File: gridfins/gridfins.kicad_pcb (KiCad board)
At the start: 4 copper layers, 195 parts, among them IC1 2536030320001, J1 RBUS, J2 USB_C_Receptacle_USB2.0, J3 ServoCH0, J4 ServoCH1, J5 ServoCH2, J6 ST1W008S4TR2000, J8 1053131104, Q1 SSM3K15AMFV,L3F, Q3 DMP3099, Q4 SSM3K15AMFV,L3F, Q5 BSZ025N04LS, Q6 BSZ025N04LS, U1 ESP32-S3, U10 LM74810, U12 SiC437AED-T1, U2 SN65HVD230, U3 LM66200DRLR, U4 MAX77827AEFD+T, U5 SC4215ASTRT, U6 SiC437AED-T1, U7 DRV8834PWP, U8 MMC5983MA, U9 H3LIS331DLTR, Y1 R940000171

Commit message: feat: Massive changes, board almost ready for review
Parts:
- removed C18: 10uF, Capacitor_SMD:C_0402_1005Metric
- removed D6, D7: ~, Package_TO_SOT_SMD:SOT-353_SC-70-5
- removed JP2, JP3: Conn_01x02_Male, Connector_PinHeader_2.54mm:PinHeader_1x02_P2.54mm_Vertical
- removed TP3: TestPoint, TestPoint:TestPoint_Pad_D1.0mm
- added C30: 10uF, Capacitor_SMD:C_0805_2012Metric, F.Cu at (225.7, 102.0)
- added D3: CPDF3V3UP-HF, iclr:CPD, B.Cu at (249.6, 67.0)
- added G**: orientation_marker, iclr-hw:orientation_marker, F.Cu at (258.4, 46.8)
- added J10: Limit switch 2, Connector_PinHeader_2.54mm:PinHeader_1x02_P2.54mm_Vertical, F.Cu at (230.3, 90.9)
- added J11: Conn_01x03_Pin, Connector_PinHeader_1.00mm:PinHeader_1x03_P1.00mm_Vertical, F.Cu at (242.7, 52.7)
- added J7: Encoder breakout, Connector_PinHeader_2.54mm:PinHeader_2x03_P2.54mm_Vertical, F.Cu at (243.8, 62.2)
- added J9: Limit switch 1, Connector_PinHeader_2.54mm:PinHeader_1x02_P2.54mm_Vertical, F.Cu at (230.3, 81.7)
- added R46: 10k, Resistor_SMD:R_0402_1005Metric, F.Cu at (238.0, 108.9)
- added R47: 10k, Resistor_SMD:R_0402_1005Metric, F.Cu at (230.3, 99.5)
- added R48: 10k, Resistor_SMD:R_0402_1005Metric, F.Cu at (230.7, 79.3)
- added R49: 10k, Resistor_SMD:R_0402_1005Metric, F.Cu at (230.7, 93.3)
- added TP11: TestPoint, TestPoint:TestPoint_Pad_D1.0mm, F.Cu at (228.2, 67.6)
- added TP12: TestPoint, TestPoint:TestPoint_Pad_D1.0mm, F.Cu at (231.7, 98.2)
- added TP13: TestPoint, TestPoint:TestPoint_Pad_D1.0mm, F.Cu at (246.3, 78.9)
- added TP14: TestPoint, TestPoint:TestPoint_Pad_D1.0mm, F.Cu at (245.5, 83.7)
- D4, D5: value ~ -> CPDF3V3UP-HF; footprint Package_TO_SOT_SMD:SOT-353_SC-70-5 -> iclr:CPD; moved to B.Cu
- J1: footprint iclr:Molex_Mini-Fit_Jr_5569-06A2_2x03_P4.20mm_Horizontal -> iclr:Molex_Mini-Fit_Jr_5569-08A2_2x04_P4.20mm_Horizontal
- J6, R25, R26, R27, R30, R56, TP1, TP2, TP25, TP26, TP27, TP4, TP5, TP6, TP7, TP8: moved to B.Cu
- JP1: footprint iclr:SmallerSolderJP -> Capacitor_SMD:C_0603_1608Metric_Pad1.08x0.95mm_HandSolder
- R43, R44: value 0.32 -> 0.5; footprint Resistor_SMD:R_0402_1005Metric -> Resistor_SMD:R_2512_6332Metric
- moved H3 171.8 mm to (254.8, 112.5)
- moved H2 167.6 mm to (254.8, 33.5)
- moved J3 165.7 mm to (252.0, 65.4)
- moved J4 165.7 mm to (252.0, 75.9)
- moved J5 165.7 mm to (252.0, 86.4)
- moved C10 157.9 mm to (251.6, 48.4), turned to 45 degrees
- moved C13 153.0 mm to (250.2, 45.8), turned to -90 degrees
- moved R25 152.1 mm to (249.5, 70.2), turned to -90 degrees
- moved C5 151.8 mm to (243.1, 50.9), turned to -90 degrees
- moved C9 151.2 mm to (245.1, 47.9), turned to 90 degrees
- moved C1 151.2 mm to (243.6, 49.5)
- moved C4 150.8 mm to (242.1, 49.4), turned to -90 degrees
- moved R26 150.7 mm to (249.5, 80.0), turned to -90 degrees
- moved R27 149.8 mm to (249.4, 88.2), turned to -90 degrees
- moved C6 149.6 mm to (245.1, 51.0), turned to 90 degrees
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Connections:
- C3 pad 1: /CHIP_PU -> GND
- C3 pad 2: GND -> /CHIP_PU
- C40 pad 1: +16.8V -> /DeployV
- C48 pad 1: +16.8V -> /DeployV
- C75 pad 1: +16.8V -> /DeployV
- C82 pad 1: +16.8V -> /DeployV
- C85 pad 1: +16.8V -> /DeployV
- C92 pad 1: +16.8V -> /DeployV
- D4 pad 1: /SERVOPWM0 -> GND
- D4 pad 2: Net-(D4-Pad2) -> /SERVOPWM1
- D5 pad 2: Net-(D4-Pad2) -> /SERVOPWM2
- J1 pad 3: RBUS_uC_V -> GND
- J1 pad 4: +16.8V -> RBUS_uC_V
- J1 pad 5: /CAN+ -> /DeployV
- J1 pad 6: /CAN- -> /DeployV
- J8 pad 1: Net-(U7-AOUT1) -> /Linear Actuator/BOUT1
- J8 pad 2: Net-(U7-AOUT2) -> /Linear Actuator/BOUT2
- J8 pad 3: Net-(U7-BOUT2) -> /Linear Actuator/AOUT2
- J8 pad 4: Net-(U7-BOUT1) -> /Linear Actuator/AOUT1
- Q1 pad 1: /BUCK_EN -> /BUCK_EN_H
- Q4 pad 1: /BUCK_EN -> /BUCK_EN_S
- R20 pad 2: /BuckPGOOD -> /BuckPGOOD_H
- R24 pad 2: /BUCK_EN -> /BUCK_EN_H
- R34 pad 2: /BuckPGOOD -> /BuckPGOOD_H
- R45 pad 2: /BuckPGOOD -> /BuckPGOOD_S
- R56 pad 2: +16.8V -> /DeployV
- R58 pad 2: /BuckPGOOD -> /BuckPGOOD_S
- R62 pad 2: /BUCK_EN -> /BUCK_EN_S
- R66 pad 2: +16.8V -> /DeployV
- R7 pad 1: +12V -> +10V
- U1 pad 10: /SD1_CS -> /VSPI_MISO
- U1 pad 13: /VSPI_MISO -> /SD1_CS
- U1 pad 14: /HSPI_MISO -> /ENCODER_CS
- U1 pad 15: /HSPI_MOSI -> /CAN_RX
- U1 pad 16: /HSPI_SCLK -> /CAN_TX
- U1 pad 17: /IMU1_CS -> /HSIDE_EN
- U1 pad 18: /IMU2_CS -> /BUCK_EN_H
- U1 pad 19: /MAG_CS -> /BUCK_EN_S
- U1 pad 21: /STEP/BENBL -> /SERVOPWM2
- U1 pad 22: /NSLEEP -> /SERVOPWM1
- U1 pad 23: /M0/APHASE -> /SERVOPWM0
- U1 pad 24: /DIR/BPHASE -> /BUS_VMON
- U1 pad 27: /NENBL/AENBL -> /M0/APHASE
- U1 pad 36: unconnected-(U1-SPICLK_N/GPIO48-Pad36) -> /M1
- U1 pad 37: unconnected-(U1-SPICLK_P/GPIO47-Pad37) -> /Fault
- U1 pad 38: unconnected-(U1-GPIO33-Pad38) -> /NSLEEP
- U1 pad 39: /SERVOPWM0 -> /DIR/BPHASE
- U1 pad 40: /SERVOPWM1 -> /STEP/BENBL
- U1 pad 41: /SERVOPWM2 -> /NENBL/AENBL
- U1 pad 42: /HSIDE_EN -> /HSPI_MOSI
- U1 pad 43: /ENCODER_CS -> /HSPI_SCLK
- U1 pad 44: unconnected-(U1-MTCK/JTAG/GPIO39-Pad44) -> /HSPI_MISO
- U1 pad 45: unconnected-(U1-MTDO/JTAG/GPIO40-Pad45) -> /Switch_1
- U1 pad 47: unconnected-(U1-MTDI/JTAG/GPIO41-Pad47) -> /IMU1_CS
- U1 pad 48: unconnected-(U1-MTMS/JTAG/GPIO42-Pad48) -> /IMU2_CS
- U1 pad 51: /BUCK_EN -> /MAG_CS
- U1 pad 6: /BUS_VMON -> /Switch_2
- U12 pad 1: +16.8V -> /DeployV
- U12 pad 14: /BuckPGOOD -> /BuckPGOOD_S
- U12 pad 2: +16.8V -> /DeployV
- U12 pad 22: +16.8V -> /DeployV
- U12 pad 26: +16.8V -> /DeployV
- U6 pad 1: +16.8V -> /DeployV
- U6 pad 14: /BuckPGOOD -> /BuckPGOOD_H
- U6 pad 2: +16.8V -> /DeployV
- U6 pad 22: +16.8V -> /DeployV
- U6 pad 26: +16.8V -> /DeployV
- U7 pad 14: /Linear Actuator/VINT -> /M1
- U7 pad 15: GND -> Net-(U7-CONFIG)
- U7 pad 16: unconnected-(U7-NFAULT-Pad16) -> /Fault
- U7 pad 4: Net-(U7-AOUT1) -> /Linear Actuator/AOUT1
- U7 pad 6: Net-(U7-AOUT2) -> /Linear Actuator/AOUT2
- U7 pad 7: Net-(U7-BOUT2) -> /Linear Actuator/BOUT2
- U7 pad 9: Net-(U7-BOUT1) -> /Linear Actuator/BOUT1
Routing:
- net /BUS_VMON: track 0.00 -> 87.1 mm, vias 0 -> 2
- net /HSIDE_EN: track 0.00 -> 77.9 mm, vias 0 -> 2
- net /Switch_1: track 0.00 -> 77.2 mm, vias 0 -> 2
- net /NSLEEP: track 0.00 -> 76.6 mm
- net /Fault: track 0.00 -> 69.3 mm
- net /NENBL/AENBL: track 0.00 -> 69.3 mm, vias 0 -> 2
- net /STEP/BENBL: track 0.00 -> 67.9 mm, vias 0 -> 2
- net /M1: track 0.00 -> 67.7 mm
- net /DIR/BPHASE: track 0.00 -> 64.3 mm, vias 0 -> 2
- net /M0/APHASE: track 0.00 -> 63.9 mm
- net /Switch_2: track 0.00 -> 58.4 mm, vias 0 -> 1
- net +3V3: track 0.00 -> 51.3 mm, vias 1 -> 23
- net /HSPI_MISO: track 0.00 -> 33.2 mm, vias 0 -> 5
- net /Data+: track 0.00 -> 33.1 mm, vias 0 -> 2
- net /SERVOPWM2: track 0.00 -> 32.3 mm, vias 0 -> 1
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- added copper zone on B.Cu, net +10V
- added copper zone on F.Cu, net +10V
- added copper zone on In2.Cu, net +3V3
- added copper zone on F.Cu, net +7.4V
- added copper zone on F.Cu, net /Buck_SERVO/SW
- added copper zone on B.Cu, net /DeployV
- added copper zone on F.Cu, net /DeployV
- added copper zone on In2.Cu, net /DeployV
- added copper zone on B.Cu, net /Linear Actuator/AOUT1
- added copper zone on F.Cu, net /Linear Actuator/AOUT1
- added copper zone on B.Cu, net /Linear Actuator/AOUT2
- added copper zone on F.Cu, net /Linear Actuator/AOUT2
- added copper zone on B.Cu, net /Linear Actuator/BOUT1
- added copper zone on F.Cu, net /Linear Actuator/BOUT1
- added copper zone on B.Cu, net /Linear Actuator/BOUT2
- added copper zone on F.Cu, net /Linear Actuator/BOUT2
- added copper zone on F.Cu, net /Linear Actuator/VREFO
- added copper zone on B.Cu, net /VOUTSwitch
- added copper zone on F.Cu, net /VOUTSwitch
- added copper zone on B.Cu, net /master high side switch/C
- added copper zone on F.Cu, net /master high side switch/C
- added copper zone on B.Cu, net GND
- added copper zone on In1.Cu, net GND
- added copper zone on F.Cu, net Net-(C6-Pad1)
- added copper zone on B.Cu, net Net-(C65-Pad2)
- added copper zone on B.Cu, net Net-(C90-Pad2)
- added copper zone on F.Cu, net Net-(JP1-B)
- added copper zone on F.Cu, net Net-(U7-AISEN)
- added copper zone on F.Cu, net Net-(U7-BISEN)
- removed copper zone on F.Cu, net +16.8V
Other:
- board outline added: 47.1 x 85.5 mm
- board text added: "LEDs"
- board text added: "connect to Voutswitch via"

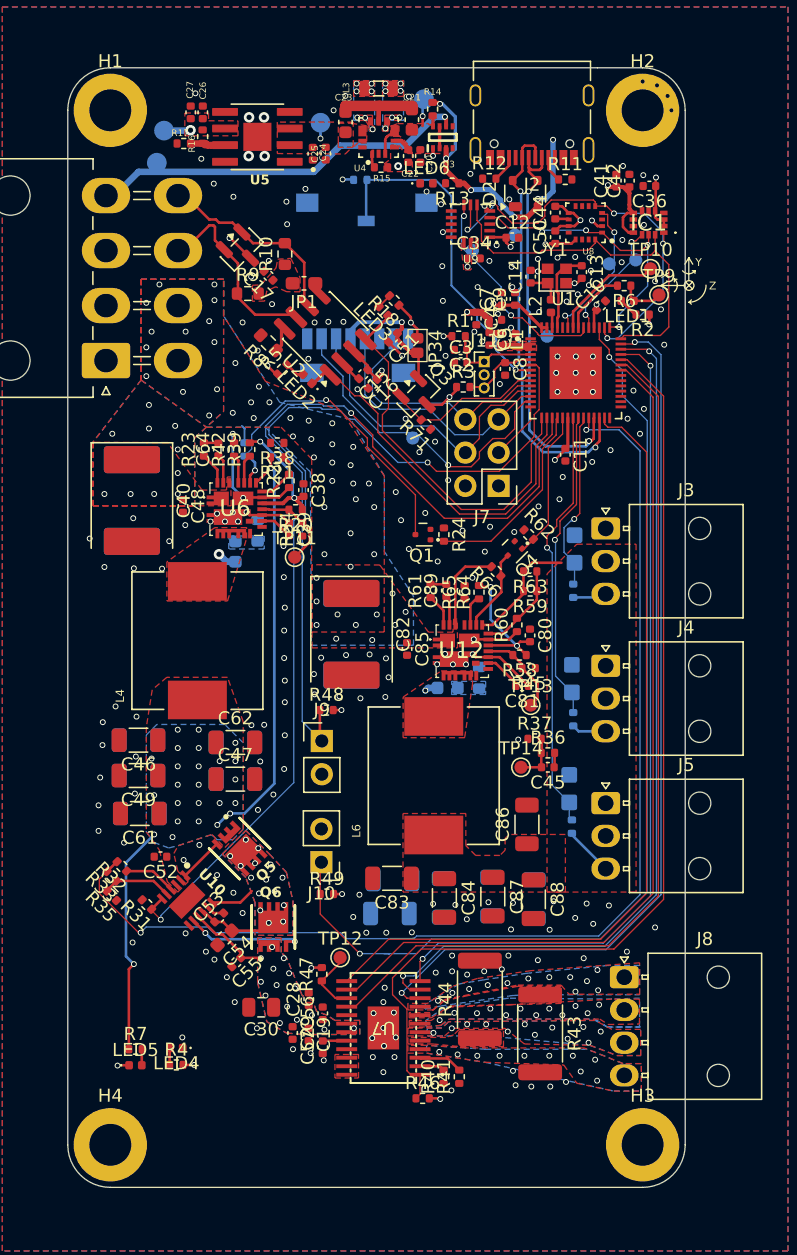
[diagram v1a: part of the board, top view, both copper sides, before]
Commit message: feat: A few more changes, mainly fixing copper pours and DRC erros. Still need to change buck inductors to wuerth ones + route end stop switch traces better.
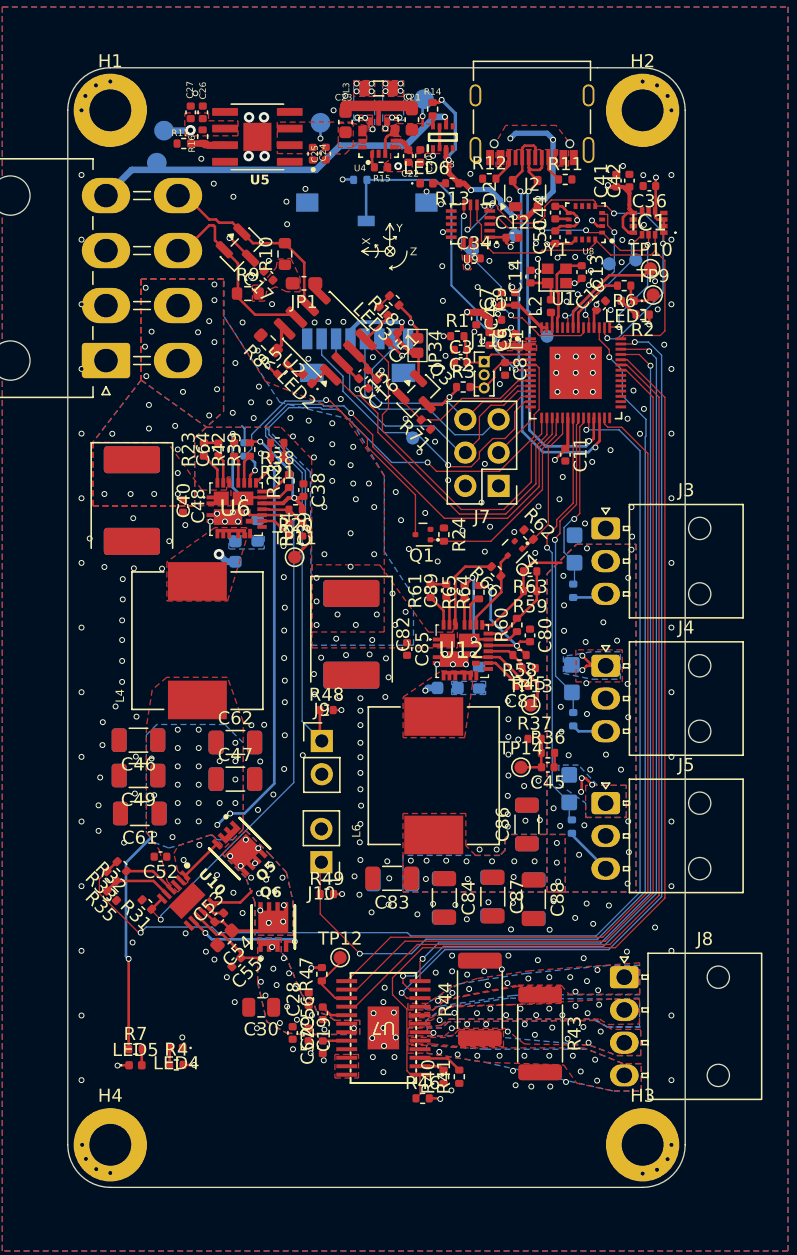
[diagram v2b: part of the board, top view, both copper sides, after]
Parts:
- moved G** 23.0 mm to (235.5, 44.2)
- moved C94 12.5 mm to (246.0, 88.0), turned to 90 degrees
- moved TP9 0.45 mm to (255.6, 47.6)
- moved R1 0.10 mm to (240.7, 50.7)
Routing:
- net GND: track 45.0 -> 214.7 mm, vias 223 -> 314
- net VBUS: track 22.3 -> 26.3 mm, vias 6 -> 7
- net Net-(U7-VCP): track 0.00 -> 2.09 mm
- net Net-(U12-_MODE_1): track 0.00 -> 1.99 mm
- net /Buck_H_bridge/FB: track 4.06 -> 5.16 mm
- net /BUCK_EN_H: track 15.1 -> 16.2 mm
- net Net-(LED6-A): track 0.00 -> 0.97 mm
- net +10V: track 50.0 -> 50.8 mm
- net /Switch_1: track 77.2 -> 76.6 mm
- net /DeployV: vias 60 -> 59
- net +7.4V: vias 0 -> 39
- added copper zone on B.Cu, net +7.4V
- added copper zone on F.Cu, net VBUS
- removed copper zone on In2.Cu, net /DeployV

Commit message: feat: Ready for first review, made a mockup name etc
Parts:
- added G***: LOGO, LOGO, F.Cu at (218.3, 103.6)
- added G***: LOGO, LOGO, B.Cu at (234.7, 85.3)
- added LOGO1: ICLR LOGO, iclr:iclr_logo_estd2018_10mm, B.Cu at (245.8, 36.3)
- moved R4 8.49 mm to (214.7, 99.2), turned to 90 degrees
- moved R7 6.51 mm to (213.5, 99.2), turned to -90 degrees
- moved LED5 2.29 mm to (216.0, 104.1)
- moved TP8 1.65 mm to (228.7, 34.9)
- moved LED4 1.54 mm to (217.9, 104.3)
- moved R40 1.23 mm to (239.6, 108.5)
- moved R41 1.15 mm to (240.8, 108.4)
- moved TP1 0.95 mm to (246.6, 50.7)
- moved R46 0.93 mm to (237.1, 108.9), turned to 180 degrees
- moved G** 0.85 mm to (235.1, 43.5), turned to 180 degrees
- moved U3 0.69 mm to (239.4, 36.2)
- moved C22 0.69 mm to (236.8, 37.6)
- moved U4 0.69 mm to (234.5, 36.2)
- moved C20 0.69 mm to (237.7, 37.6)
- moved C21 0.69 mm to (237.0, 34.9)
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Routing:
- net GND: track 214.7 -> 297.8 mm, vias 314 -> 344
- net +10V: track 50.8 -> 45.0 mm
- net Net-(LED5-A): track 1.24 -> 5.69 mm
- net Net-(LED4-A): track 1.31 -> 5.70 mm
- net /HSPI_MISO: track 33.2 -> 30.6 mm, vias 5 -> 3
- net VBUS: track 26.3 -> 24.3 mm
- net Net-(U7-BDECAY): track 1.92 -> 3.00 mm
- net /MAG_CS: track 11.2 -> 12.2 mm
- net Net-(U7-ADECAY): track 3.39 -> 4.18 mm
- net /Power/BBOUT: track 1.20 -> 1.88 mm
- net /IMU2_CS: track 16.8 -> 17.4 mm
- net /Buck_H_bridge/VDD: track 10.8 -> 11.4 mm
- net /Power/LX2: vias 7 -> 6
- net /Power/LX1: vias 7 -> 6
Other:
- board text added: "GIGA CHAD V1.0"

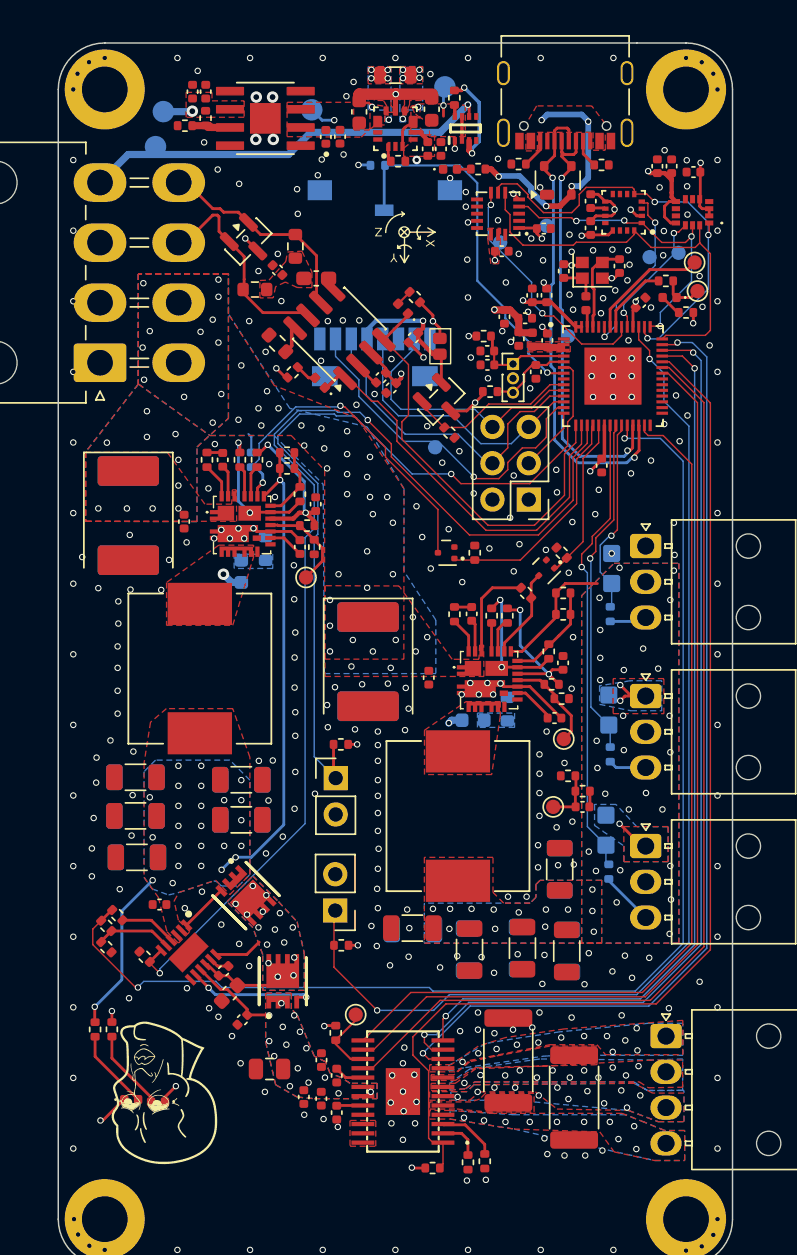
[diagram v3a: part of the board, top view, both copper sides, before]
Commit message: feat: Smoothed the traces + fixed some zone issues and disconnected VBUS issue.
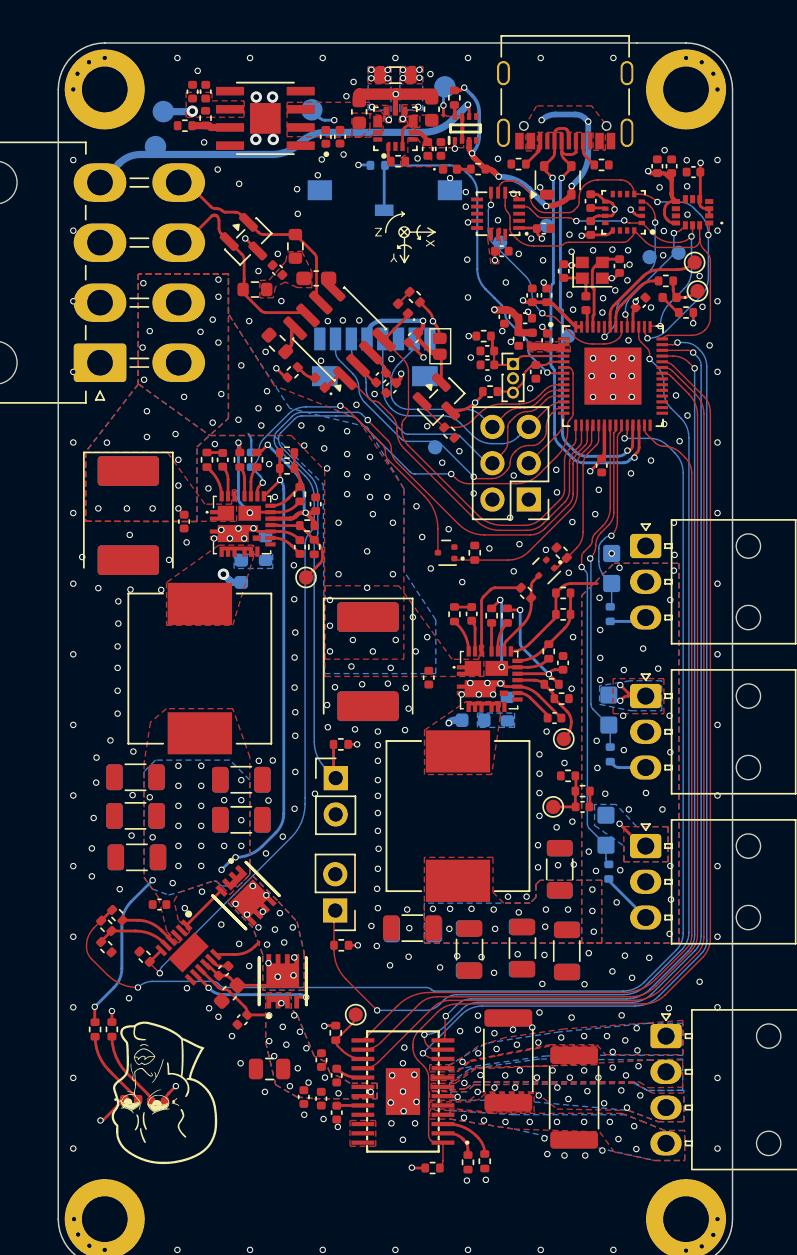
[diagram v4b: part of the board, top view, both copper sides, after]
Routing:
- net /HSIDE_EN: track 77.9 -> 76.9 mm
- net /SERVOPWM0: track 13.8 -> 14.7 mm
- net /Switch_2: track 58.4 -> 57.5 mm
- net /HSPI_MISO: track 30.6 -> 31.5 mm
- net /Switch_1: track 76.5 -> 75.8 mm
- net +3V3: track 51.1 -> 50.4 mm
- net /Buck_H_bridge/EN: track 24.6 -> 23.9 mm
- net /M0/APHASE: track 64.0 -> 63.4 mm
- net /CAN_TX: track 29.2 -> 28.6 mm
- net /CAN_RX: track 30.3 -> 29.8 mm
- net /VSPI_MOSI: track 23.1 -> 22.6 mm
- net /SD1_CS: track 24.5 -> 24.0 mm
- net /VSPI_SCLK: track 19.4 -> 18.9 mm
- net /Fault: track 69.4 -> 68.8 mm
- net /NENBL/AENBL: track 69.5 -> 68.9 mm
